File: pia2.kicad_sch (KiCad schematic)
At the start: 41 parts, among them IC25 LM393P, IC31 74LS02N, IC34 MC14050BCP, IC35 MC6821

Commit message: revise bom
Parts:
- TR1: DigiKey KSD1616AYTACT-ND -> SS8050DTACT-ND; Note use KSD1616AYTA instead -> do NOT use KSD1616AYTA instead
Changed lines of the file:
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@@
       (effects (font (size 1.27 1.27) italic) (justify left) hide)
     )
-    (property "Datasheet" "http://www.farnell.com/datasheets/296634.pdf" (at 239.649 147.32 0)
+    (property "Datasheet" "https://alltransistors.com/adv/pdfview.php?doc=bc140_bc141_cnv_2.pdf&dire=_philips" (at 239.649 147.32 0)
       (effects (font (size 1.27 1.27)) (justify left) hide)
     )
-    (property "DigiKey" "KSD1616AYTACT-ND" (at 239.649 147.32 0)
+    (property "DigiKey" "SS8050DTACT-ND" (at 239.649 147.32 0)
       (effects (font (size 1.27 1.27)) hide)
     )
-    (property "Note" "use KSD1616AYTA instead" (at 239.649 147.32 0)
+    (property "Note" "do NOT use KSD1616AYTA instead" (at 239.649 147.32 0)
       (effects (font (size 1.27 1.27)) hide)
     )

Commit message: update bom references
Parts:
- IC35: DigiKey 2156-MC6821CS-2156-ND -> (none); Mouser (none) -> 517-4840-6000-CP
- JP11-12, JP9-10: Mouser (none) -> 538-22-28-5033
- PL4: DigiKey (none) -> CP-7050-ND
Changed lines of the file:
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@@
+			)
+		)
+		(property "DigiKey" "CP-7050-ND"
+			(at 123.698 172.085 0)
+			(effects
+				(font
+					(size 1.27 1.27)
+				)
+				(hide yes)
 			)
 		)
@@
 			)
 		)
+		(property "Mouser" "538-22-28-5033"
+			(at 105.029 76.962 90)
+			(effects
+				(font
+					(size 1.27 1.27)
+				)
+				(hide yes)
+			)
+		)
 		(pin "1"
 		)
@@
 			)
 		)
+		(property "Mouser" "538-22-28-5033"
+			(at 91.44 40.132 90)
+			(effects
+				(font
+					(size 1.27 1.27)
+				)
+				(hide yes)
+			)
+		)
 		(pin "1"
 		)
@@
 			)
 		)
-		(property "DigiKey" "2156-MC6821CS-2156-ND"
+		(property "DigiKey" ""
 			(at 59.69 64.262 0)
 			(effects
@@
 			(at 59.69 64.262 0)
 			(effects
+				(font
+					(size 1.27 1.27)
+				)
+				(hide yes)
+			)
+		)
+		(property "Mouser" "517-4840-6000-CP"
+			(at 59.69 64.262 0)
+			(effects

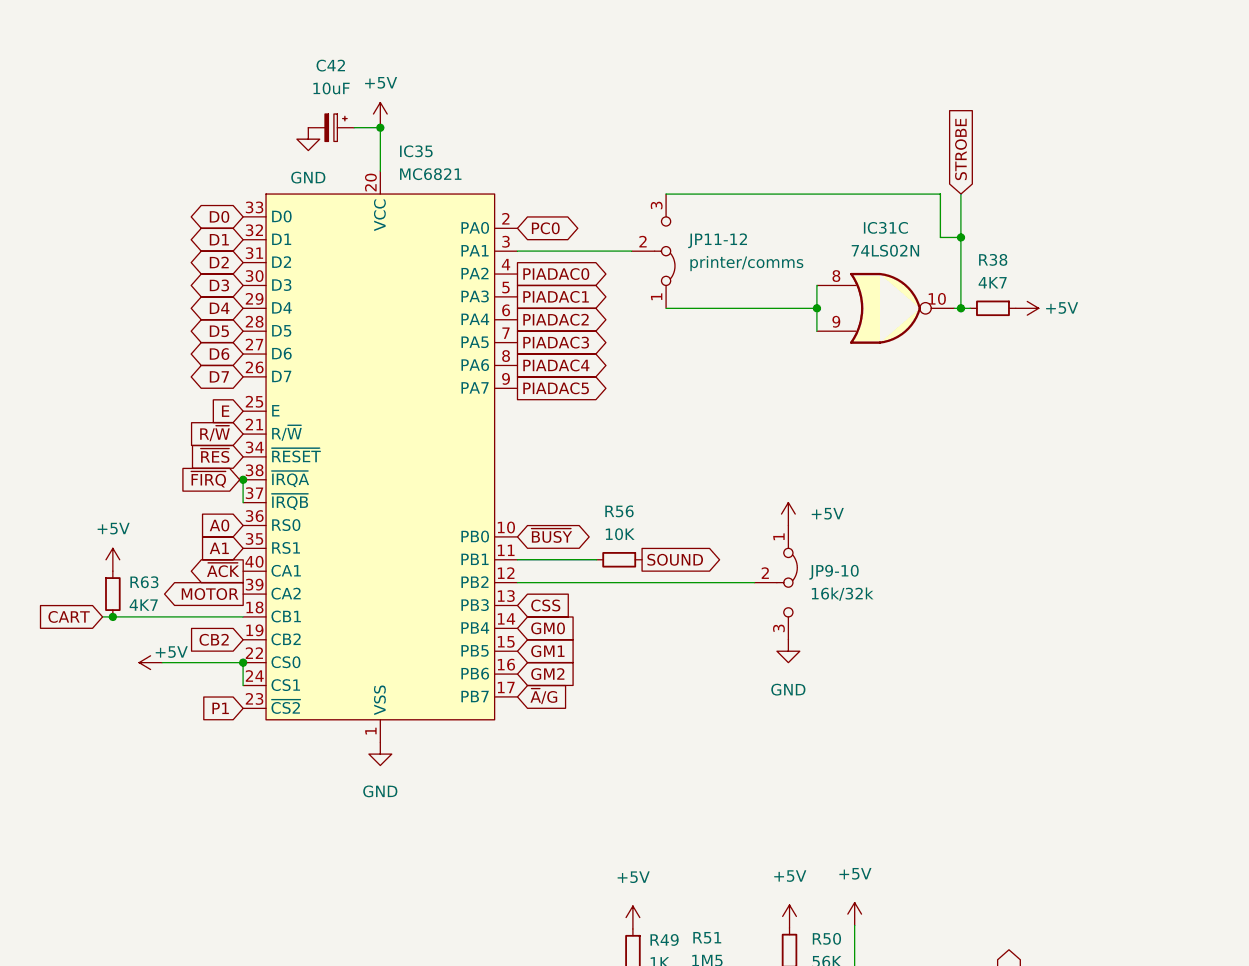
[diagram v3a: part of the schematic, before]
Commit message: fix parallel strobe inverter bypass
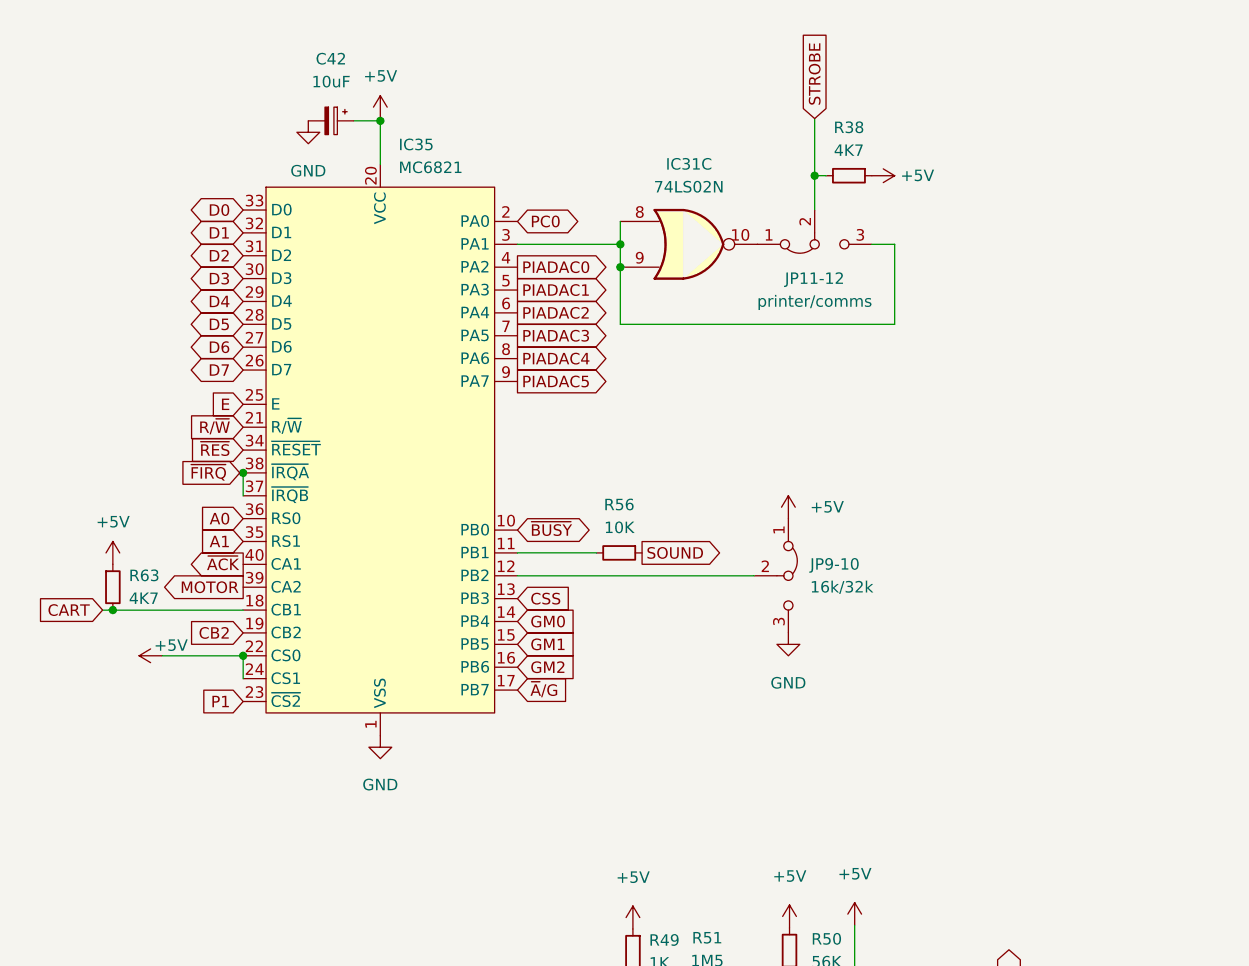
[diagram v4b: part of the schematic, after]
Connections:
- net STROBE: now also JP11-12.2 (C); no longer IC31.10, JP11-12.3 (B)
- net at IC31.8, IC31.9: now also IC35.3 (PA1), JP11-12.3 (B); no longer JP11-12.1 (A)
- new net: IC31.10, JP11-12.1 (A)
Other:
- company: (none) -> Dragon Data
- moved on the sheet: C42, IC31C, IC35, JP11-12, JP9-10, R38, R56, R63
